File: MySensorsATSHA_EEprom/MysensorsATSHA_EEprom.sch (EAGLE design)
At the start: 4 parts

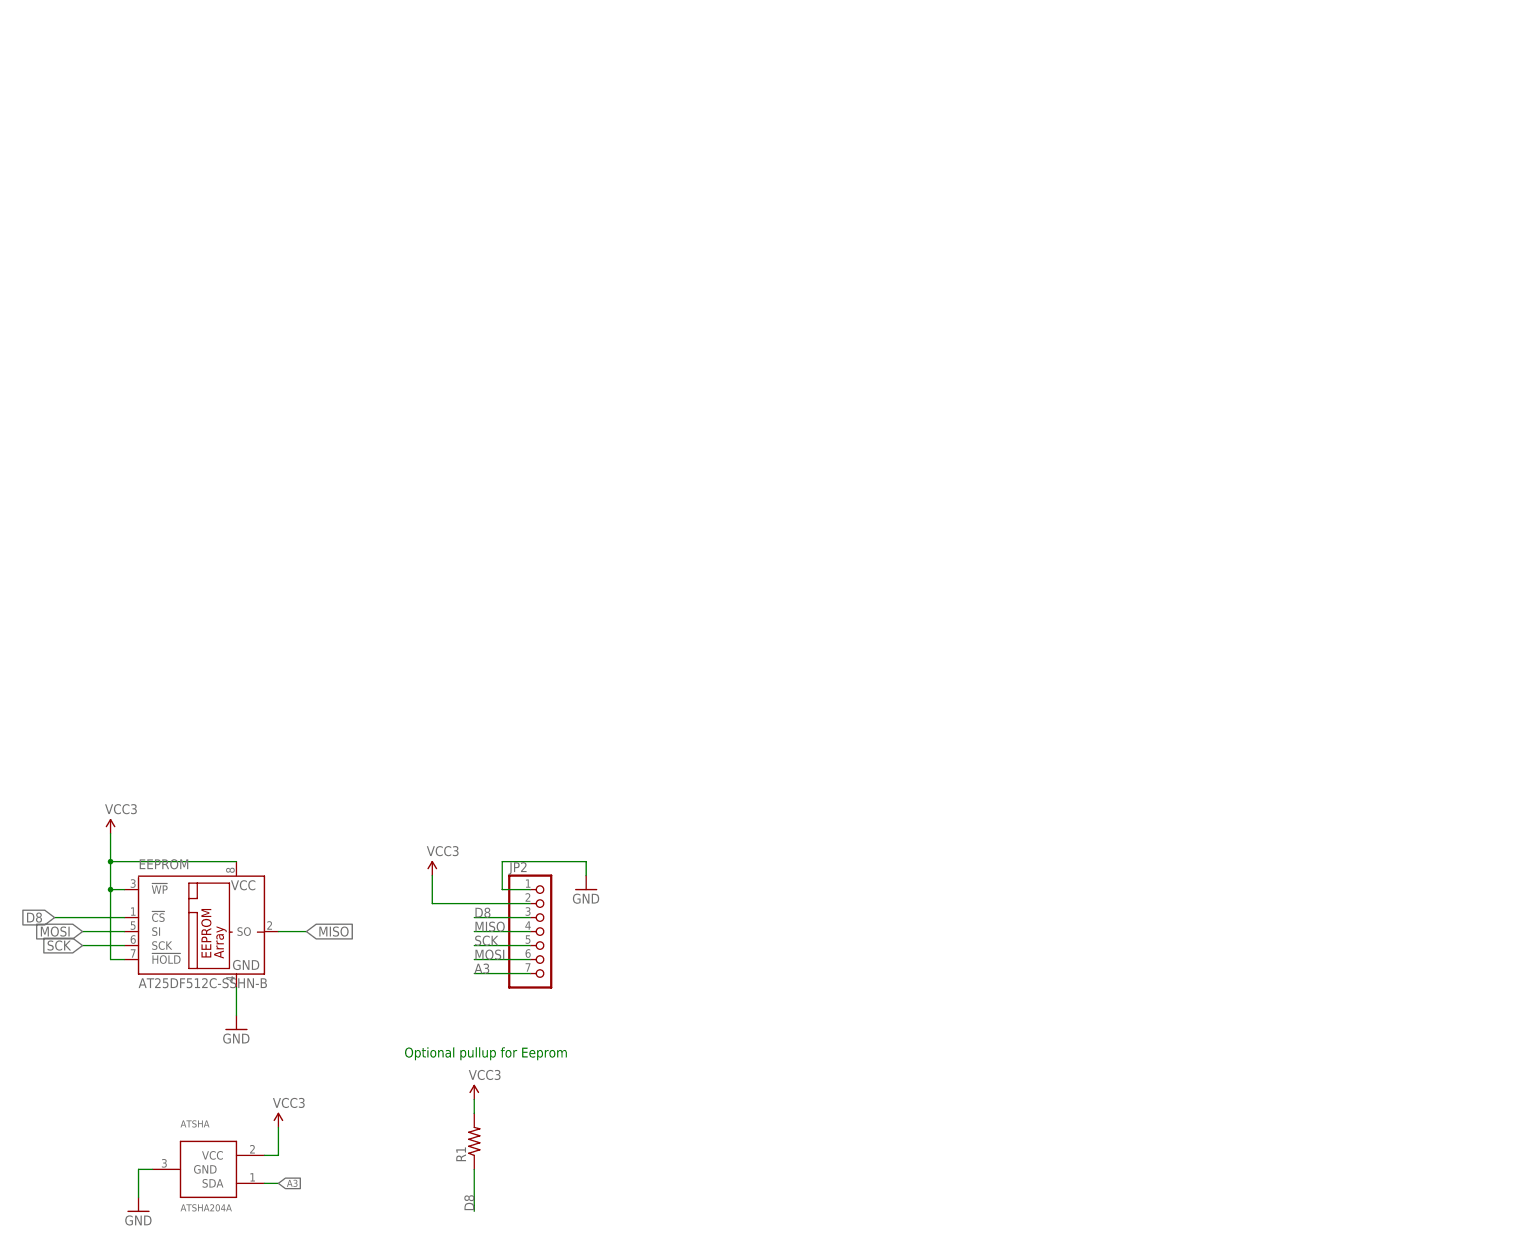
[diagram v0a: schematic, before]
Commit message: silkscreen updated, bom added
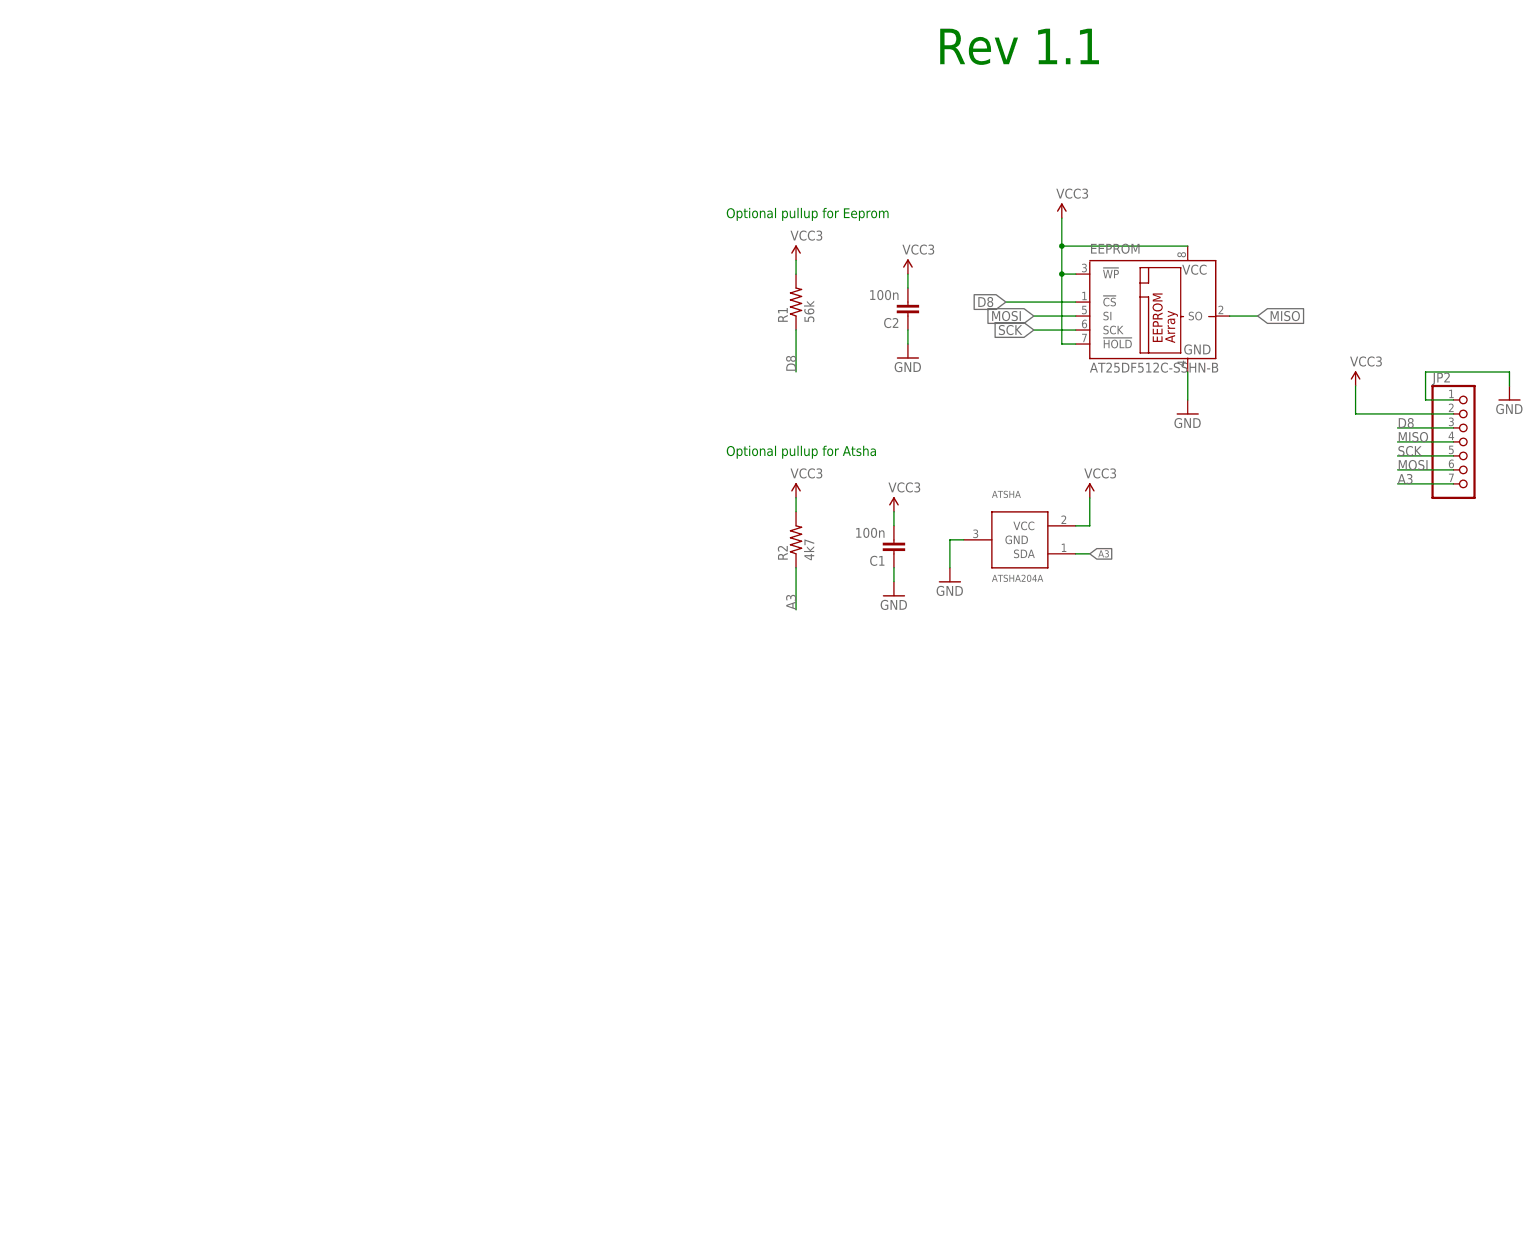
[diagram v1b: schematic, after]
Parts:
- added C1, C2: 100n, LowPowerLab:CAP1206
- added R2: 4k7, SparkFun-Resistors:RESISTOR1206
- R1: value (none) -> 56k
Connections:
- net A3: now also R2.1
- net GND: now also C1.1, C2.1
- net VCC: now also C1.2, C2.2, R2.2
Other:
- note added: "Optional pullup for Atsha"
- note added: "Rev 1.1"
- moved on the sheet: ATSHA, EEPROM, JP2, R1
